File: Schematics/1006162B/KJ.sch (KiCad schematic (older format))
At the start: 1 part

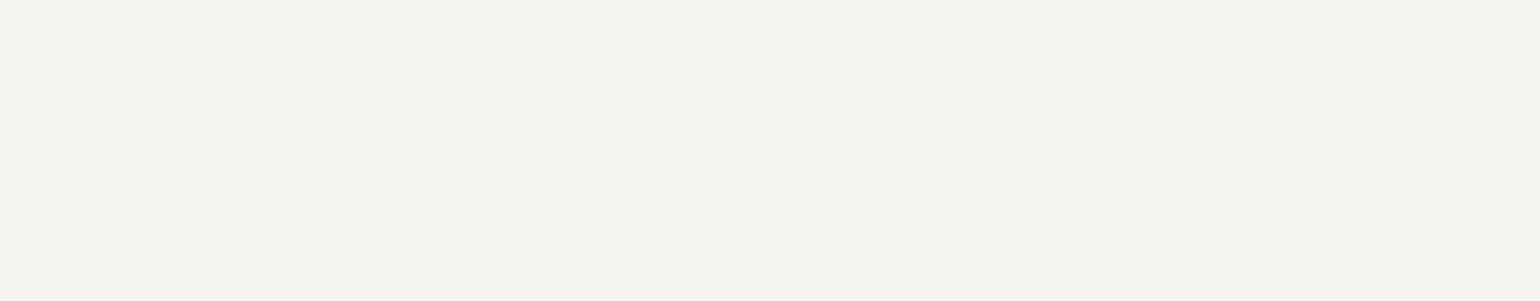
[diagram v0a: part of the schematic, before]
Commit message: Finished CAD transcription of drawing 1006162B.  Had to tweak my hierarchical-block annotator a little bit because it turns out that when KiCad annotates, it doesn't mark blocks that appear only once the same what that it marks blocks that appear more than once.
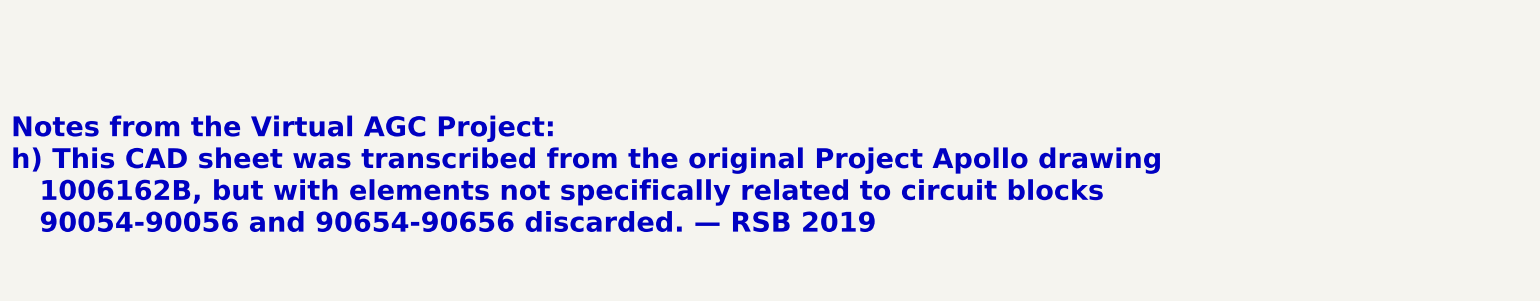
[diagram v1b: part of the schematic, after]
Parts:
- gave numbers to parts that had none: 1
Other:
- note added: "Notes from the Virtual AGC Project:\nh) This CAD sheet was transcribed from the original Project Apollo drawing\n 1006162B, but with elements not specifically related to circuit blocks\n 90054-90056 and 90654-90656 discarded. — RSB 2019\n"
